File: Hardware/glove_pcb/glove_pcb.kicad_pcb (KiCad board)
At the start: 2 copper layers, 150 x 150 mm, 106 parts, among them J1 Barrel_Jack_Switch, J10 ICSP, J11 IMU, J12 IMU, J13 Conn_01x01, J2 Conn_01x02, J3 Conn_01x02, J4 Conn_01x02, J5 Conn_01x02, J6 Conn_01x02, J7 Potentiometers, J8 Potentiometers, J9 Debug Serial, U1 AP63205WU, U10 MCP3008, U11 MCP3008, U12 BM70BLES1FC2-0B04AA, U13 74LVC1T45GW_125, U14 74LVC1T45GW_125, U2 TCR2EF33_LMCT, U3 DRV8876PWPR, U4 DRV8876PWPR, U5 DRV8876PWPR, U6 DRV8876PWPR, U7 DRV8876PWPR, U8 MCP3008, U9 ATmega328PB-A

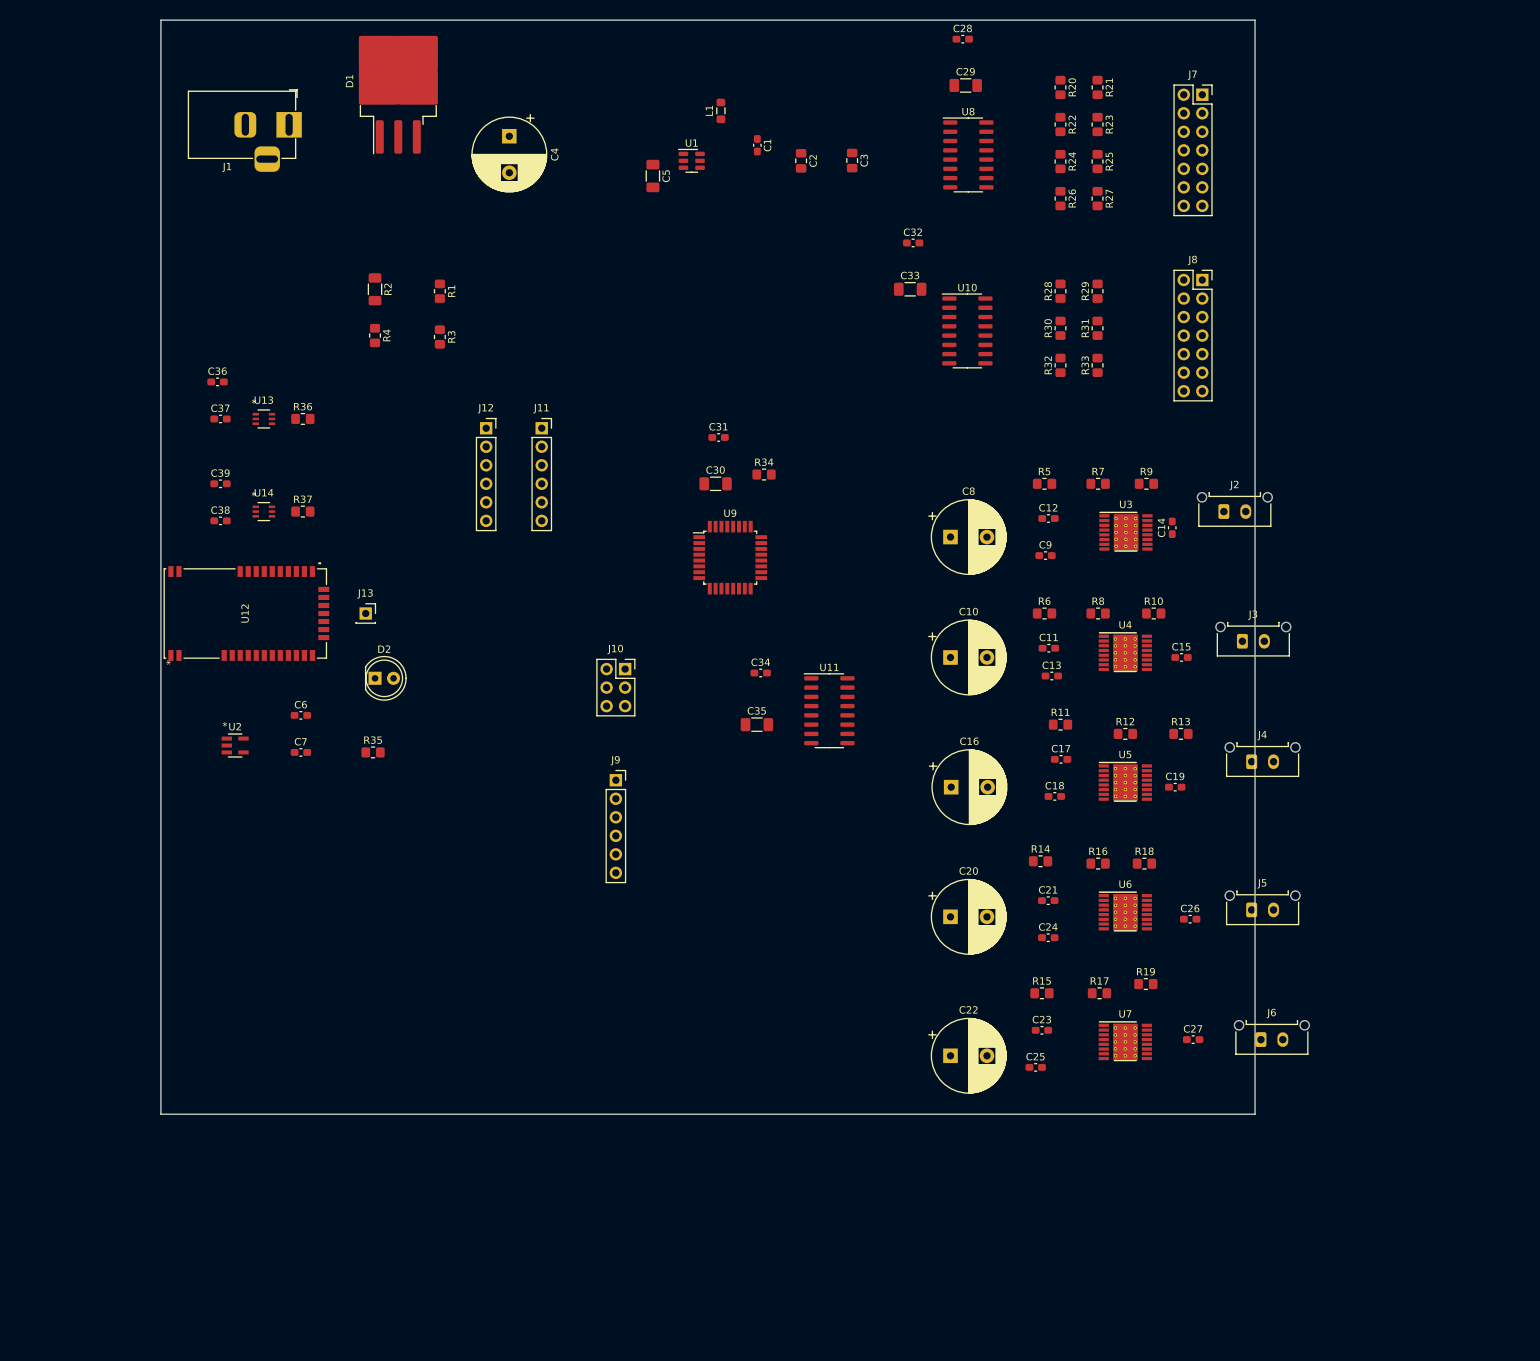
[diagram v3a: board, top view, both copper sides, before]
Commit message: Assign footprints and import all parts into pcb editor
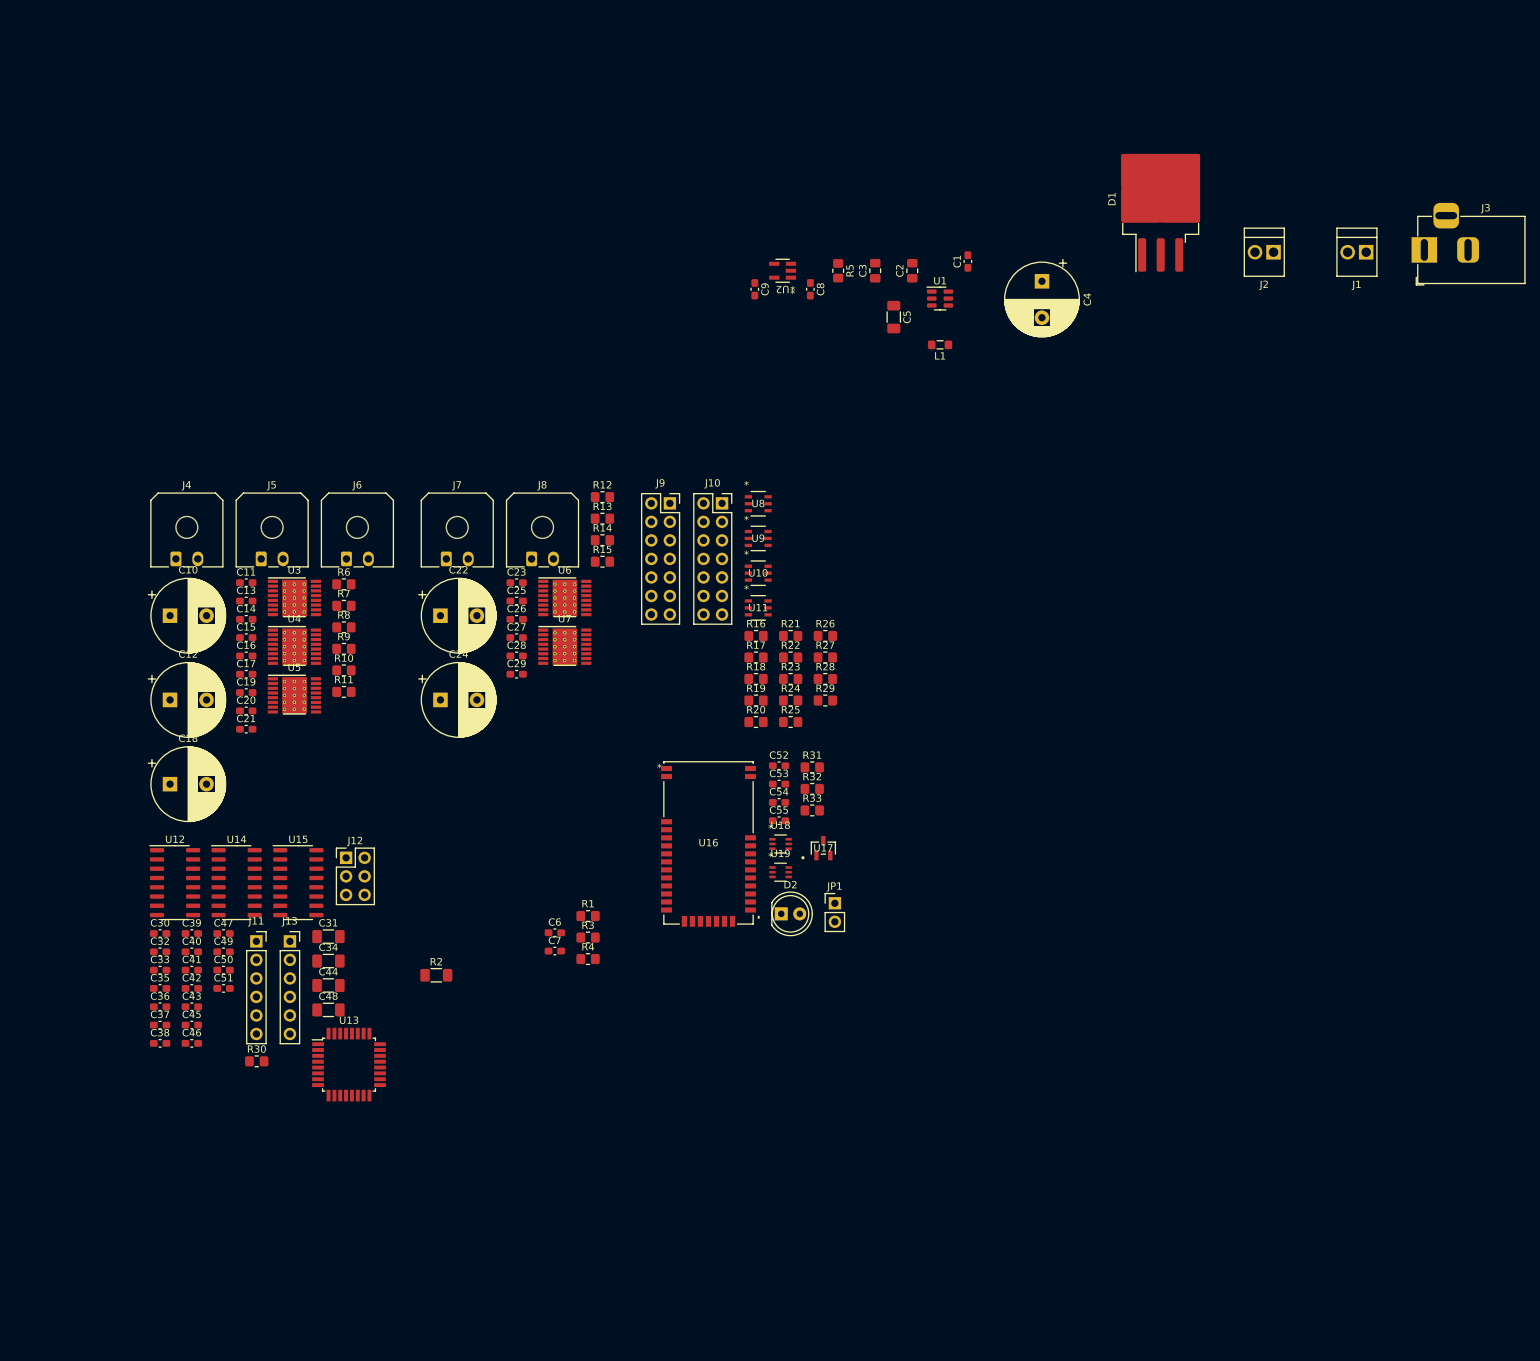
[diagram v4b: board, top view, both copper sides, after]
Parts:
- removed R34, R36, R37: 10k, Resistor_SMD:R_0805_2012Metric_Pad1.20x1.40mm_HandSolder
- removed R35: 240, Resistor_SMD:R_0805_2012Metric_Pad1.20x1.40mm_HandSolder
- added C40: 0.1uF, Capacitor_SMD:C_0603_1608Metric_Pad1.08x0.95mm_HandSolder, F.Cu at (43.5, 145.4)
- added C41: 0.1uF, Capacitor_SMD:C_0603_1608Metric_Pad1.08x0.95mm_HandSolder, F.Cu at (43.5, 148.0)
- added C42: 0.1uF, Capacitor_SMD:C_0603_1608Metric_Pad1.08x0.95mm_HandSolder, F.Cu at (43.5, 150.5)
- added C43: 0.1uF, Capacitor_SMD:C_0603_1608Metric_Pad1.08x0.95mm_HandSolder, F.Cu at (43.5, 153.0)
- added C44: 10uF, Capacitor_SMD:C_1206_3216Metric_Pad1.33x1.80mm_HandSolder, F.Cu at (62.2, 150.1)
- added C45: 0.1uF, Capacitor_SMD:C_0603_1608Metric_Pad1.08x0.95mm_HandSolder, F.Cu at (43.5, 155.5)
- added C46: 0.1uF, Capacitor_SMD:C_0603_1608Metric_Pad1.08x0.95mm_HandSolder, F.Cu at (43.5, 158.0)
- added C47: 0.1uF, Capacitor_SMD:C_0603_1608Metric_Pad1.08x0.95mm_HandSolder, F.Cu at (47.8, 142.9)
- added C48: 10uF, Capacitor_SMD:C_1206_3216Metric_Pad1.33x1.80mm_HandSolder, F.Cu at (62.2, 153.4)
- added C49: 0.1uF, Capacitor_SMD:C_0603_1608Metric_Pad1.08x0.95mm_HandSolder, F.Cu at (47.8, 145.4)
- added C50: 0.1uF, Capacitor_SMD:C_0603_1608Metric_Pad1.08x0.95mm_HandSolder, F.Cu at (47.8, 148.0)
- added C51: 0.1uF, Capacitor_SMD:C_0603_1608Metric_Pad1.08x0.95mm_HandSolder, F.Cu at (47.8, 150.5)
- added C52: 0.1uF, Capacitor_SMD:C_0603_1608Metric_Pad1.08x0.95mm_HandSolder, F.Cu at (124.0, 119.9)
- added C53: 0.1uF, Capacitor_SMD:C_0603_1608Metric_Pad1.08x0.95mm_HandSolder, F.Cu at (124.0, 122.5)
- added C54: 0.1uF, Capacitor_SMD:C_0603_1608Metric_Pad1.08x0.95mm_HandSolder, F.Cu at (124.0, 125.0)
- added C55: 0.1uF, Capacitor_SMD:C_0603_1608Metric_Pad1.08x0.95mm_HandSolder, F.Cu at (124.0, 127.5)
- added JP1: Jumper_2_Open, Connector_PinHeader_2.54mm:PinHeader_1x02_P2.54mm_Vertical, F.Cu at (131.6, 138.8)
- added U15: MCP3008, Package_SO:SOIC-16_3.9x9.9mm_P1.27mm, F.Cu at (58.1, 136.0)
- added U16: BM70BLES1FC2-0B04AA, Glove_Footprints:BM70BLES1FC2_MCH, F.Cu at (114.3, 130.5)
- added U17: MCP111T-195I/TT, Glove_Footprints:SOT-23_MC_MCH, F.Cu at (130.0, 131.2)
- added U18: 74LVC1T45GW_125, Glove_Footprints:TSSOP6_SOT363-2_NEX, F.Cu at (124.2, 130.7)
- added U19: 74LVC1T45GW_125, Glove_Footprints:TSSOP6_SOT363-2_NEX, F.Cu at (124.2, 134.5)
- C10, C22, C4: value 1mF -> 1000uF
- C12, C18, C24: value 0.1uF -> 1000uF; footprint Capacitor_SMD:C_0603_1608Metric_Pad1.08x0.95mm_HandSolder -> Capacitor_THT:CP_Radial_D10.0mm_P5.00mm
- C14, C15, C19, C26, C27: value 0.022uF -> 0.1uF
- C16: value 1mF -> 0.022uF; footprint Capacitor_THT:CP_Radial_D10.0mm_P5.00mm -> Capacitor_SMD:C_0603_1608Metric_Pad1.08x0.95mm_HandSolder
- C17, C21, C28: value 0.1uF -> 0.022uF
- C20, C8: value 1mF -> 0.1uF; footprint Capacitor_THT:CP_Radial_D10.0mm_P5.00mm -> Capacitor_SMD:C_0603_1608Metric_Pad1.08x0.95mm_HandSolder
- C29: value 10uF -> 0.022uF; footprint Capacitor_SMD:C_1206_3216Metric_Pad1.33x1.80mm_HandSolder -> Capacitor_SMD:C_0603_1608Metric_Pad1.08x0.95mm_HandSolder
- C30, C33, C35: value 10uF -> 0.1uF; footprint Capacitor_SMD:C_1206_3216Metric_Pad1.33x1.80mm_HandSolder -> Capacitor_SMD:C_0603_1608Metric_Pad1.08x0.95mm_HandSolder
- C31, C34: value 0.1uF -> 10uF; footprint Capacitor_SMD:C_0603_1608Metric_Pad1.08x0.95mm_HandSolder -> Capacitor_SMD:C_1206_3216Metric_Pad1.33x1.80mm_HandSolder
- D1: value D_Schottky -> VS-6TQ045STRL-M3
- J1: value Barrel_Jack_Switch -> OSTVN02A150; footprint Connector_BarrelJack:BarrelJack_Horizontal -> Glove_Footprints:TerminalBlock_OnShore_OSTVN02A150_P2.54mm
- J10: value ICSP -> 302-R141; footprint Connector_PinSocket_2.54mm:PinSocket_2x03_P2.54mm_Vertical -> Connector_PinSocket_2.54mm:PinSocket_2x07_P2.54mm_Vertical
- J11: value IMU -> 61300611121
- J12: value IMU -> 67997-206HLF; footprint Connector_PinSocket_2.54mm:PinSocket_1x06_P2.54mm_Vertical -> Connector_PinHeader_2.54mm:PinHeader_2x03_P2.54mm_Vertical
- J13: value Conn_01x01 -> 22053061; footprint Connector_PinSocket_2.54mm:PinSocket_1x01_P2.54mm_Vertical -> Connector_PinSocket_2.54mm:PinSocket_1x06_P2.54mm_Vertical
- J2: value Conn_01x02 -> OSTVN02A150; footprint Connector_Molex:Molex_Micro-Fit_3.0_43650-0215_1x02_P3.00mm_Vertical -> Glove_Footprints:TerminalBlock_OnShore_OSTVN02A150_P2.54mm
- J3: value Conn_01x02 -> 54-00130; footprint Connector_Molex:Molex_Micro-Fit_3.0_43650-0215_1x02_P3.00mm_Vertical -> Connector_BarrelJack:BarrelJack_Horizontal
- J4, J5, J6: value Conn_01x02 -> 0436500200; footprint Connector_Molex:Molex_Micro-Fit_3.0_43650-0215_1x02_P3.00mm_Vertical -> Connector_Molex:Molex_Micro-Fit_3.0_43650-0200_1x02_P3.00mm_Horizontal
- J7, J8: value Potentiometers -> 0436500200; footprint Connector_PinSocket_2.54mm:PinSocket_2x07_P2.54mm_Vertical -> Connector_Molex:Molex_Micro-Fit_3.0_43650-0200_1x02_P3.00mm_Horizontal
- J9: value Debug Serial -> 302-R141; footprint Connector_PinSocket_2.54mm:PinSocket_1x06_P2.54mm_Vertical -> Connector_PinSocket_2.54mm:PinSocket_2x07_P2.54mm_Vertical
- R10, R13: value 3.6k -> 10k
- R11, R14, R15, R8: value 10k -> 3.6k
- R16, R17: value 10k -> 1k
- R18, R19: value 3.6k -> 1k
- R30, R32, R33: value 1k -> 10k
- R31: value 1k -> 240
- U10, U11, U8: value MCP3008 -> BZA408B; footprint Package_SO:SOIC-16_3.9x9.9mm_P1.27mm -> Glove_Footprints:SOT457_NXP
- U12: value BM70BLES1FC2-0B04AA -> MCP3008; footprint Glove_Footprints:BM70BLES1FC2_MCH -> Package_SO:SOIC-16_3.9x9.9mm_P1.27mm
- U13: value 74LVC1T45GW_125 -> ATmega328PB-A; footprint Glove_Footprints:TSSOP6_SOT363-2_NEX -> Package_QFP:TQFP-32_7x7mm_P0.8mm
- U14: value 74LVC1T45GW_125 -> MCP3008; footprint Glove_Footprints:TSSOP6_SOT363-2_NEX -> Package_SO:SOIC-16_3.9x9.9mm_P1.27mm
- U9: value ATmega328PB-A -> BZA408B; footprint Package_QFP:TQFP-32_7x7mm_P0.8mm -> Glove_Footprints:SOT457_NXP
- moved J4 150.1 mm to (41.3, 91.6)
- moved R30 149.1 mm to (52.4, 160.5), turned to 0 degrees
- moved J1 148.7 mm to (204.5, 49.5), turned to 180 degrees
- moved J5 144.1 mm to (53.0, 91.6)
- moved C32 141.8 mm to (39.1, 145.4)
- moved J6 141.6 mm to (64.7, 91.6)
- moved C33 138.9 mm to (39.1, 148.0)
- moved C15 128.3 mm to (50.9, 102.4)
- moved C19 128.0 mm to (50.9, 109.9)
- moved C14 127.6 mm to (50.9, 99.9), turned to 0 degrees
- moved C12 123.0 mm to (40.5, 110.9)
- moved J7 121.6 mm to (78.4, 91.6)
- moved C18 121.3 mm to (40.5, 122.5)
- moved U5 114.6 mm to (57.5, 110.3)
- moved U3 114.4 mm to (57.5, 96.9)
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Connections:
- C10 pad 1: MOTOR_VM -> +12V
- C11 pad 1: MOTOR_VM -> +12V
- C12 pad 1: MOTOR_VM -> +12V
- C12 pad 2: Net-(U3-VCP) -> GND
- C13 pad 1: MOTOR_VM -> +12V
- C13 pad 2: Net-(U4-VCP) -> GND
- C14 pad 1: Net-(U3-CPH) -> +12V
- C14 pad 2: Net-(U3-CPL) -> Net-(U3-VCP)
- C15 pad 1: Net-(U4-CPH) -> +12V
- C15 pad 2: Net-(U4-CPL) -> Net-(U4-VCP)
- C16 pad 1: MOTOR_VM -> Net-(U3-CPH)
- C16 pad 2: GND -> Net-(U3-CPL)
- C17 pad 1: MOTOR_VM -> Net-(U4-CPH)
- C17 pad 2: GND -> Net-(U4-CPL)
- C18 pad 1: MOTOR_VM -> +12V
- C18 pad 2: Net-(U5-VCP) -> GND
- C19 pad 1: Net-(U5-CPH) -> +12V
- C19 pad 2: Net-(U5-CPL) -> GND
- C2 pad 1: VCC_UC -> +5V
- C20 pad 1: MOTOR_VM -> +12V
- C20 pad 2: GND -> Net-(U5-VCP)
- C21 pad 1: MOTOR_VM -> Net-(U5-CPH)
- C21 pad 2: GND -> Net-(U5-CPL)
- C22 pad 1: MOTOR_VM -> +12V
- C23 pad 1: MOTOR_VM -> +12V
- C24 pad 1: MOTOR_VM -> +12V
- C24 pad 2: Net-(U6-VCP) -> GND
- C25 pad 1: MOTOR_VM -> +12V
- C25 pad 2: Net-(U7-VCP) -> GND
- C26 pad 1: Net-(U6-CPH) -> +12V
- C26 pad 2: Net-(U6-CPL) -> Net-(U6-VCP)
- C27 pad 1: Net-(U7-CPH) -> +12V
- C27 pad 2: Net-(U7-CPL) -> Net-(U7-VCP)
- C28 pad 1: VCC_UC -> Net-(U6-CPH)
- C28 pad 2: GND -> Net-(U6-CPL)
- C29 pad 1: VCC_UC -> Net-(U7-CPH)
- C29 pad 2: GND -> Net-(U7-CPL)
- C3 pad 1: VCC_UC -> +5V
- C30 pad 1: VCC_UC -> GND
- C30 pad 2: GND -> POT_THUMB_1
- C31 pad 1: VCC_UC -> +5V
- C32 pad 1: VCC_UC -> +5V
- C33 pad 1: VCC_UC -> +5V
- C34 pad 1: VCC_UC -> +5V
- C35 pad 1: VCC_UC -> GND
- C35 pad 2: GND -> POT_THUMB_2
- C36 pad 1: VCC_UC -> GND
- C36 pad 2: GND -> POT_INDEX_1
- C37 pad 1: VCC_BT -> GND
- C37 pad 2: GND -> POT_INDEX_2
- C38 pad 1: VCC_BT -> GND
- C38 pad 2: GND -> POT_INDEX_3
- C39 pad 1: VCC_UC -> GND
- C39 pad 2: GND -> POT_MIDDLE_1
- C4 pad 1: MOTOR_VM -> +12V
- C5 pad 1: MOTOR_VM -> +12V
- C6 pad 1: VCC_UC -> POT_AREF
- C7 pad 1: VCC_BT -> MOTOR_AREF
- C8 pad 1: MOTOR_VM -> +5V
- C9 pad 1: MOTOR_VM -> +3.3V
- D1 pad 2: MOTOR_VM -> +12V
- J1 pad 1: Net-(D1-A) -> Net-(J1-Pin_1)
- J1 pad 2: GND -> Net-(J1-Pin_2)
- J10 pad 1: MISO -> GND
- J10 pad 2: SCK -> POT_MIDDLE_3
- J10 pad 3: RST -> GND
- J10 pad 4: VCC_UC -> POT_RING_1
- J10 pad 5: MOSI -> GND
- J10 pad 6: GND -> POT_RING_2
- J11 pad 2: MOSI1 -> MISO
- J11 pad 3: SCK1 -> MOSI
- J11 pad 4: GND -> unconnected-(J11-Pin_4-Pad4)
- J11 pad 6: VCC_UC -> GND
- J12 pad 1: SS_IMU -> MISO
- J12 pad 2: MISO1 -> +5V
- J12 pad 3: GND -> SCK
- J12 pad 4: unconnected-(J12-Pin_4-Pad4) -> MOSI
- J12 pad 5: unconnected-(J12-Pin_5-Pad5) -> RST
- J12 pad 6: unconnected-(J12-Pin_6-Pad6) -> GND
- J13 pad 1: Net-(J13-Pin_1) -> GND
- J2 pad 1: Net-(J2-Pin_1) -> Net-(J1-Pin_2)
- J2 pad 2: Net-(J2-Pin_2) -> Net-(D1-A)
- J3 pad 1: Net-(J3-Pin_1) -> Net-(J1-Pin_1)
- J3 pad 2: Net-(J3-Pin_2) -> GND
- J7 pad 1: GND -> Net-(J7-Pin_1)
- J7 pad 2: POT_THUMB_1 -> Net-(J7-Pin_2)
- J8 pad 1: GND -> Net-(J8-Pin_1)
- J8 pad 2: POT_MIDDLE_3 -> Net-(J8-Pin_2)
- J9 pad 1: unconnected-(J9-Pin_1-Pad1) -> GND
- J9 pad 2: MISO -> POT_THUMB_1
- J9 pad 3: MOSI -> GND
- J9 pad 4: unconnected-(J9-Pin_4-Pad4) -> POT_THUMB_2
- J9 pad 5: unconnected-(J9-Pin_5-Pad5) -> GND
- J9 pad 6: GND -> POT_INDEX_1
- L1 pad 2: VCC_UC -> +5V
- R1 pad 1: VCC_UC -> +5V
- R10 pad 1: MOTOR2_ISEN -> MOTOR3_FAULT
- R10 pad 2: GND -> +5V
- R11 pad 1: MOTOR3_FAULT -> MOTOR3_ISEN
- R11 pad 2: VCC_UC -> GND
- R12 pad 1: UC_MOTOR_PMODE -> MOTOR4_FAULT
- R12 pad 2: GND -> +5V
- R13 pad 1: MOTOR3_ISEN -> MOTOR5_FAULT
- R13 pad 2: GND -> +5V
- R14 pad 1: MOTOR4_FAULT -> MOTOR4_ISEN
- R14 pad 2: VCC_UC -> GND
- R15 pad 1: MOTOR5_FAULT -> MOTOR5_ISEN
- R15 pad 2: VCC_UC -> GND
- R16 pad 1: UC_MOTOR_PMODE -> +5V
- R16 pad 2: GND -> POT_THUMB_1
- R17 pad 1: UC_MOTOR_PMODE -> +5V
- R17 pad 2: GND -> POT_THUMB_2
- R18 pad 1: MOTOR4_ISEN -> +5V
- R18 pad 2: GND -> POT_INDEX_1
- R19 pad 1: MOTOR5_ISEN -> +5V
- R19 pad 2: GND -> POT_INDEX_2
- R2 pad 1: VCC_UC -> +5V
- R20 pad 1: VCC_UC -> +5V
- R20 pad 2: POT_THUMB_1 -> POT_INDEX_3
- R21 pad 1: VCC_UC -> +5V
- R21 pad 2: POT_THUMB_2 -> POT_MIDDLE_1
- R22 pad 1: VCC_UC -> +5V
- R22 pad 2: POT_INDEX_1 -> POT_MIDDLE_2
- R23 pad 1: VCC_UC -> +5V
- R23 pad 2: POT_INDEX_2 -> POT_MIDDLE_3
- R24 pad 1: VCC_UC -> POT_RING_1
- R24 pad 2: POT_INDEX_3 -> +5V
- R25 pad 1: VCC_UC -> POT_RING_2
- R25 pad 2: POT_MIDDLE_1 -> +5V
- R26 pad 1: VCC_UC -> POT_RING_3
- R26 pad 2: POT_MIDDLE_2 -> +5V
- R27 pad 1: VCC_UC -> POT_PINKY_1
- R27 pad 2: POT_MIDDLE_3 -> +5V
- R28 pad 1: POT_RING_1 -> POT_PINKY_2
- R28 pad 2: VCC_UC -> +5V
- R29 pad 1: POT_RING_2 -> +5V
- R29 pad 2: VCC_UC -> POT_PINKY_3
- R30 pad 1: POT_RING_3 -> +5V
- R30 pad 2: VCC_UC -> RST
- R31 pad 1: POT_PINKY_1 -> +3.3V
- R31 pad 2: VCC_UC -> Net-(D2-A)
- R32 pad 1: POT_PINKY_2 -> +3.3V
- R32 pad 2: VCC_UC -> Net-(U16-RST_N)
- R33 pad 1: VCC_UC -> +5V
- R33 pad 2: POT_PINKY_3 -> Net-(U19-DIR)
- R5 pad 1: MOTOR1_FAULT -> Net-(U2-CONTROL)
- R5 pad 2: VCC_UC -> +5V
- R6 pad 1: MOTOR2_FAULT -> MOTOR1_FAULT
- R6 pad 2: VCC_UC -> +5V
- R7 pad 1: UC_MOTOR_PMODE -> MOTOR2_FAULT
- R7 pad 2: GND -> +5V
- R8 pad 1: UC_MOTOR_PMODE -> MOTOR1_ISEN
- R9 pad 1: MOTOR1_ISEN -> MOTOR2_ISEN
- U1 pad 1: VCC_UC -> +5V
- U1 pad 2: MOTOR_VM -> +12V
- U1 pad 3: MOTOR_VM -> +12V
- U10 pad 1: POT_RING_1 -> POT_PINKY_3
- U10 pad 2: POT_RING_2 -> GND
- U10 pad 3: POT_RING_3 -> POT_PINKY_2
- U10 pad 5: POT_PINKY_2 -> GND
- U10 pad 6: POT_PINKY_3 -> POT_RING_3
- U11 pad 1: MOTOR1_ISEN -> POT_RING_2
- U11 pad 2: MOTOR2_ISEN -> GND
- U11 pad 3: MOTOR3_ISEN -> POT_RING_1
- U11 pad 4: MOTOR4_ISEN -> POT_MIDDLE_3
- U11 pad 5: MOTOR5_ISEN -> GND
- U11 pad 6: unconnected-(U11-CH5-Pad6) -> GND
- U12 pad 1: GND -> POT_THUMB_1
- U12 pad 10: unconnected-(U12-BK_O-Pad10) -> SS_ADC1
- U12 pad 11: unconnected-(U12-P2_7/TX_IND-Pad11) -> MOSI1
- U12 pad 12: unconnected-(U12-P1_1-Pad12) -> MISO1
- U12 pad 13: unconnected-(U12-P1_2/SCL-Pad13) -> SCK1
- U12 pad 14: unconnected-(U12-P1_3/SDA-Pad14) -> GND
- U12 pad 15: unconnected-(U12-P0_0/CTS-Pad15) -> POT_AREF
- U12 pad 16: unconnected-(U12-P1_0-Pad16) -> +5V
- U12 pad 2: GND -> POT_THUMB_2
- U12 pad 3: GND -> POT_INDEX_1
- U12 pad 4: VCC_BT -> POT_INDEX_2
- U12 pad 5: unconnected-(U12-P2_2-Pad5) -> POT_INDEX_3
- U12 pad 6: unconnected-(U12-VDD_IO-Pad6) -> POT_MIDDLE_1
- U12 pad 7: unconnected-(U12-VDD_IO-Pad7) -> POT_MIDDLE_2
- U12 pad 8: unconnected-(U12-ULPC_O-Pad8) -> POT_MIDDLE_3
- U12 pad 9: unconnected-(U12-P2_3-Pad9) -> GND
- U13 pad 1: VCC_UC -> OC2B
- U13 pad 2: GND -> MOTOR5_FAULT
- U13 pad 3: RXD -> MOTOR3_FAULT
- U13 pad 4: 3V3_RXD -> +5V
- U13 pad 5: Net-(U13-DIR) -> GND
- U13 pad 6: VCC_BT -> MOTOR4_FAULT
- U14 pad 1: VCC_UC -> POT_RING_1
- U14 pad 2: GND -> POT_RING_2
- U14 pad 3: TXD -> POT_RING_3
- U14 pad 4: 3V3_TXD -> POT_PINKY_1
- U14 pad 5: Net-(U14-DIR) -> POT_PINKY_2
- U14 pad 6: VCC_BT -> POT_PINKY_3
- U2 pad 1: VCC_UC -> +5V
- U2 pad 3: VCC_UC -> Net-(U2-CONTROL)
- U2 pad 5: VCC_BT -> +3.3V
- U3 pad 10: Net-(J2-Pin_2) -> Net-(J4-Pin_2)
- U3 pad 11: MOTOR_VM -> +12V
- U3 pad 16: UC_MOTOR_PMODE -> GND
- U3 pad 8: Net-(J2-Pin_1) -> Net-(J4-Pin_1)
- U4 pad 10: Net-(J3-Pin_2) -> Net-(J5-Pin_2)
- U4 pad 11: MOTOR_VM -> +12V
- U4 pad 16: UC_MOTOR_PMODE -> GND
- U4 pad 2: UC_MOTOR_PH1 -> UC_MOTOR_PH2
- U4 pad 8: Net-(J3-Pin_1) -> Net-(J5-Pin_1)
- U5 pad 10: Net-(J4-Pin_2) -> Net-(J6-Pin_2)
- U5 pad 11: MOTOR_VM -> +12V
- U5 pad 16: UC_MOTOR_PMODE -> GND
- U5 pad 8: Net-(J4-Pin_1) -> Net-(J6-Pin_1)
- U6 pad 10: Net-(J5-Pin_2) -> Net-(J7-Pin_2)
- U6 pad 11: MOTOR_VM -> +12V
- U6 pad 16: UC_MOTOR_PMODE -> GND
- U6 pad 2: UC_MOTOR_PH2 -> UC_MOTOR_PH3
- U6 pad 8: Net-(J5-Pin_1) -> Net-(J7-Pin_1)
- U7 pad 10: Net-(J6-Pin_2) -> Net-(J8-Pin_2)
- U7 pad 11: MOTOR_VM -> +12V
- U7 pad 16: UC_MOTOR_PMODE -> GND
- U7 pad 2: UC_MOTOR_PH2 -> UC_MOTOR_PH3
- U7 pad 8: Net-(J6-Pin_1) -> Net-(J8-Pin_1)
- U8 pad 2: POT_THUMB_2 -> GND
- U8 pad 3: POT_INDEX_1 -> POT_THUMB_2
- U8 pad 4: POT_INDEX_2 -> POT_INDEX_3
- U8 pad 5: POT_INDEX_3 -> GND
- U8 pad 6: POT_MIDDLE_1 -> POT_INDEX_2
- U9 pad 1: OC2B -> POT_INDEX_3
- U9 pad 2: MOTOR5_FAULT -> GND
- U9 pad 3: MOTOR3_FAULT -> POT_MIDDLE_1
- U9 pad 4: VCC_UC -> POT_MIDDLE_2
- U9 pad 6: MOTOR4_FAULT -> GND
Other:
- board outline removed

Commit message: Minor changes
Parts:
- moved R6 65.7 mm to (63.7, 29.4)
- moved R8 65.7 mm to (63.7, 35.3)
- moved C16 64.3 mm to (44.0, 41.0), turned to 90 degrees
- moved J8 59.8 mm to (30.3, 94.5), turned to 90 degrees
- moved C14 54.9 mm to (49.0, 45.0), turned to 180 degrees
- moved U3 52.8 mm to (40.4, 47.0)
- moved C10 52.8 mm to (55.0, 48.6), turned to -90 degrees
- moved J7 48.7 mm to (30.3, 83.5), turned to 90 degrees
- moved C11 46.2 mm to (45.0, 49.0), turned to -90 degrees
- moved J4 42.5 mm to (30.3, 50.5), turned to 90 degrees
- moved J6 39.3 mm to (30.3, 72.5), turned to 90 degrees
- moved J5 37.7 mm to (30.3, 61.5), turned to 90 degrees
- moved C12 30.1 mm to (45.3, 81.2)
- moved C13 30.1 mm to (55.7, 67.6)
- moved C15 30.1 mm to (55.7, 72.7)
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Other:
- copper layers 2 -> 4
